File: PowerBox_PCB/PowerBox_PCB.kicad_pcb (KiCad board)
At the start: 2 copper layers, 120 x 85 mm, 112 parts, among them SW1 SW_DPDT_x2, U10 BQ25887RGER

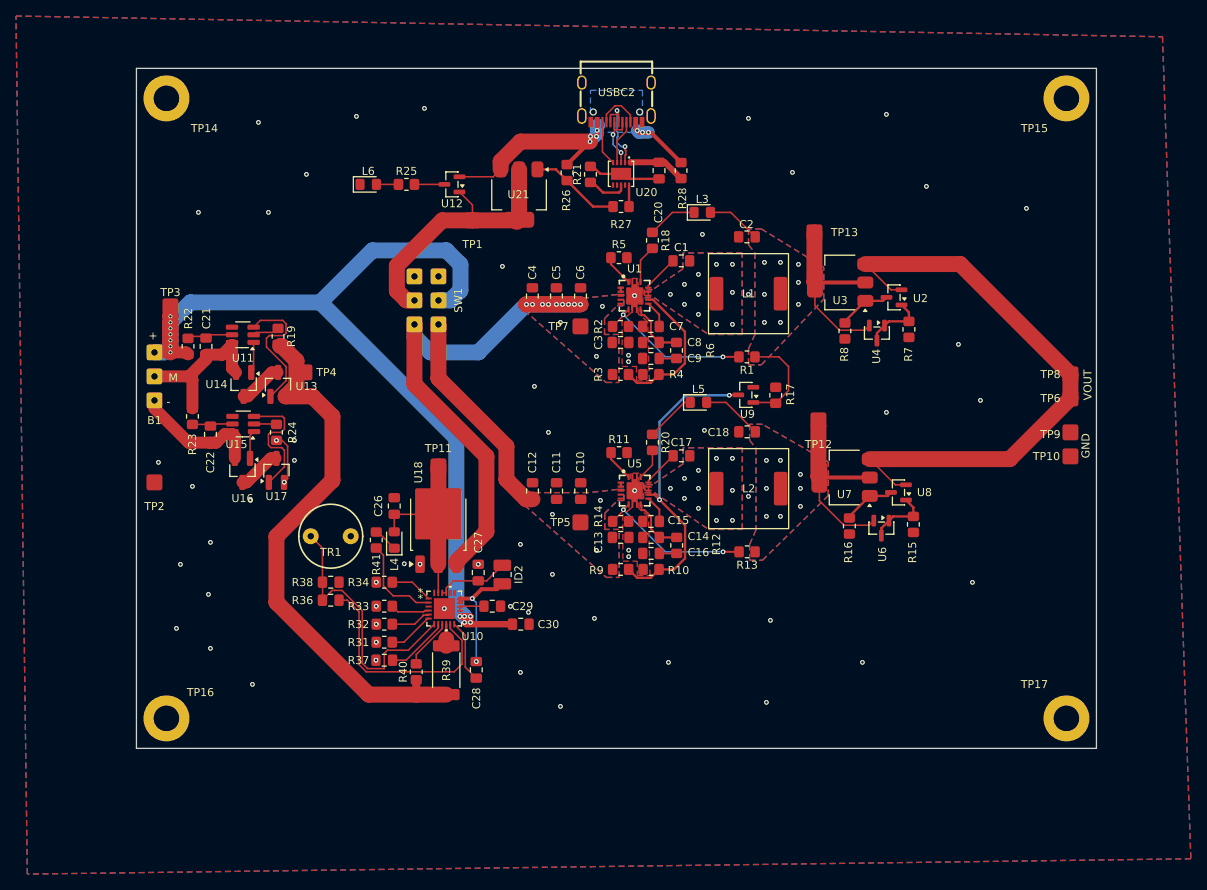
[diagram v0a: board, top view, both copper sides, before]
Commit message: made board a lot smaller
board is now 100 x 75 mm
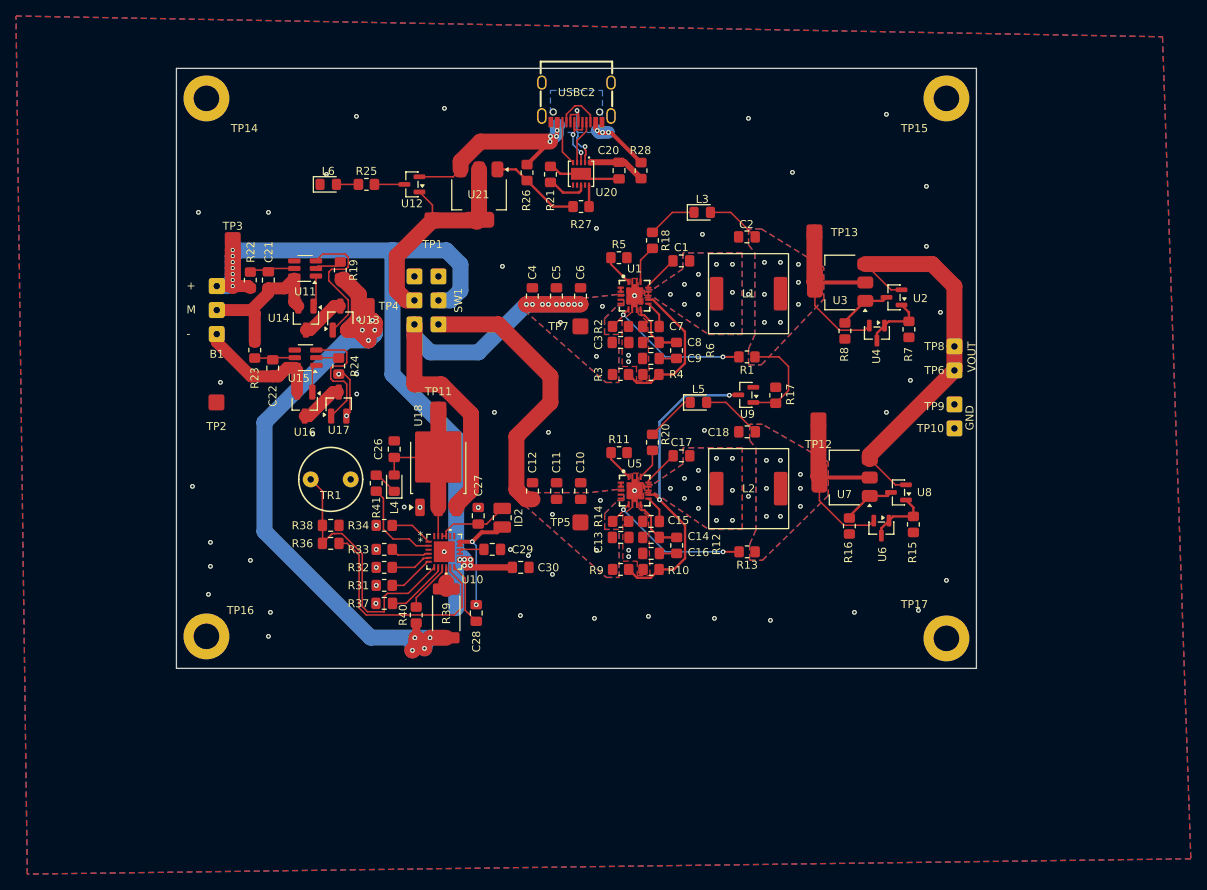
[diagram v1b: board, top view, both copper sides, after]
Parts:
- moved TP17 18.0 mm to (151.2, 121.2)
- moved TP15 15.0 mm to (151.2, 53.8)
- moved TP10 14.9 mm to (152.2, 95.0)
- moved TP6 14.9 mm to (152.2, 87.8)
- moved TP8 14.9 mm to (152.2, 84.8)
- moved TP9 14.9 mm to (152.2, 92.0)
- moved TP2 12.7 mm to (60.0, 91.8)
- moved TP16 11.4 mm to (58.8, 121.0)
- moved U15 11.4 mm to (71.1, 86.2)
- moved U11 11.4 mm to (71.1, 75.0)
- moved B1 11.4 mm to (60.0, 80.2)
- moved TP3 11.4 mm to (62.0, 71.5)
- moved U13 11.4 mm to (71.2, 81.2)
- moved C21 11.4 mm to (66.5, 76.5)
- moved C22 11.4 mm to (67.0, 87.5)
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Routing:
- net /Ideal_Diode/VOUT_IDEAL: track 74.3 -> 50.0 mm
- net PM: track 68.7 -> 92.0 mm, vias 0 -> 9
- net P+: track 120.8 -> 112.4 mm
- net /TPS54620_Buck1/VIN_BUCK: track 27.2 -> 35.1 mm
- net /VUSBPDSWITCHED: track 67.6 -> 60.9 mm
- net VUSBPD: track 34.4 -> 30.1 mm
- net GND: vias 61 -> 60
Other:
- board size 120 x 85 mm -> 100 x 75 mm
